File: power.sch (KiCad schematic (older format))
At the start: 6 parts

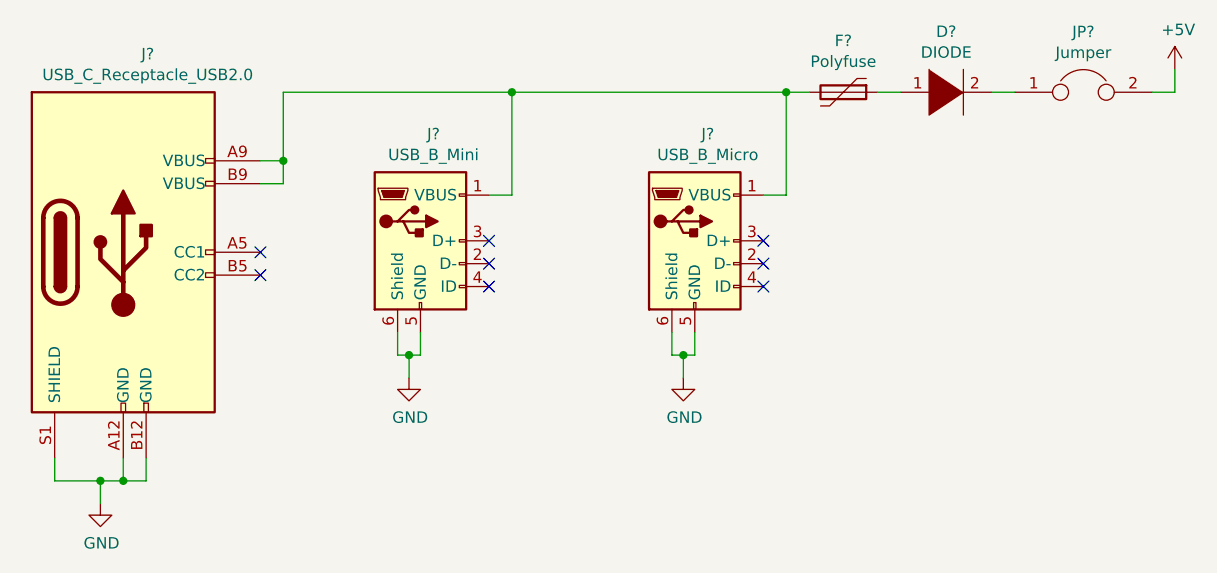
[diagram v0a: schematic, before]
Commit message: Joystick net assigned.
Signed-off-by: Kali Prasad <kprasadvnsi@protonmail.com>
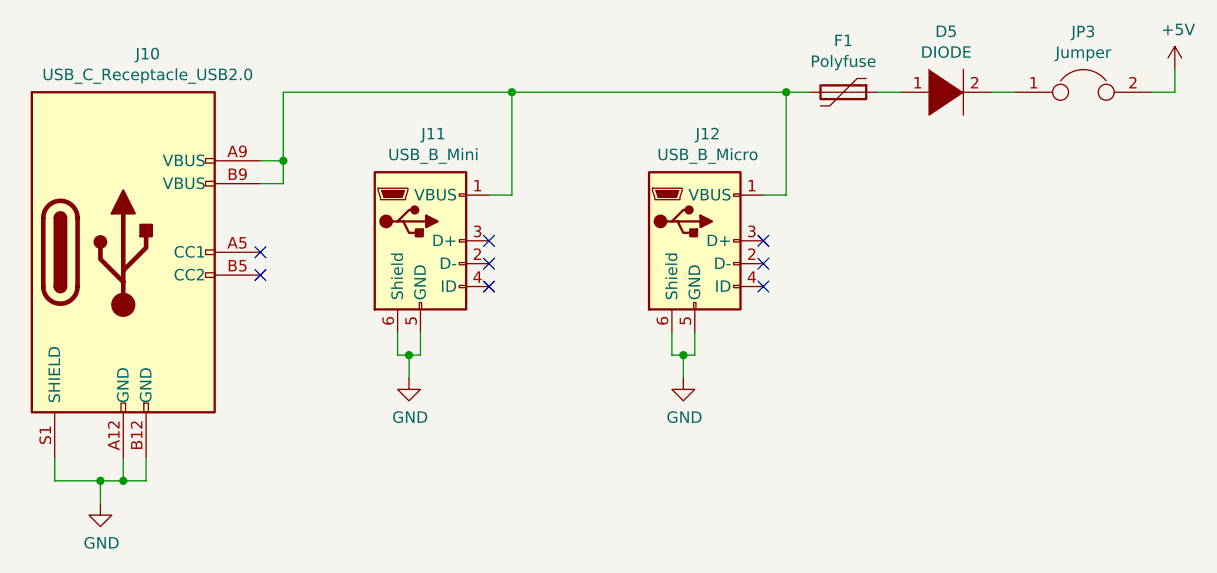
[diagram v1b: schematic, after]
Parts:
- gave numbers to parts that had none: 6
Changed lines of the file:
@@
 $EndDescr
 $Comp
-L lt_eval_board:USB_C_Receptacle_USB2.0 J?
+L lt_eval_board:USB_C_Receptacle_USB2.0 J10
 U 1 1 5D177E87
 P 3650 3950
-F 0 "J?" H 3757 4817 50  0000 C CNN
+F 0 "J10" H 3757 4817 50  0000 C CNN
 F 1 "USB_C_Receptacle_USB2.0" H 3757 4726 50  0000 C CNN
 F 2 "" H 3800 3950 50  0001 C CNN
@@
 $EndComp
 $Comp
-L Connector:USB_B_Mini J?
+L Connector:USB_B_Mini J11
 U 1 1 5D178582
 P 4950 3900
-F 0 "J?" H 5007 4367 50  0000 C CNN
+F 0 "J11" H 5007 4367 50  0000 C CNN
 F 1 "USB_B_Mini" H 5007 4276 50  0000 C CNN
 F 2 "" H 5100 3850 50  0001 C CNN
@@
 $EndComp
 $Comp
-L Connector:USB_B_Micro J?
+L Connector:USB_B_Micro J12
 U 1 1 5D178CFA
 P 6150 3900
-F 0 "J?" H 6207 4367 50  0000 C CNN
+F 0 "J12" H 6207 4367 50  0000 C CNN
 F 1 "USB_B_Micro" H 6207 4276 50  0000 C CNN
 F 2 "" H 6300 3850 50  0001 C CNN
@@
 $EndComp
 $Comp
-L power:GND #PWR?
+L power:GND #PWR045
 U 1 1 5D17D7B7
 P 3550 5050
-F 0 "#PWR?" H 3550 4800 50  0001 C CNN
+F 0 "#PWR045" H 3550 4800 50  0001 C CNN
 F 1 "GND" H 3555 4877 50  0000 C CNN
 F 2 "" H 3550 5050 50  0001 C CNN
@@
 $EndComp
 $Comp
-L power:GND #PWR?
+L power:GND #PWR046
 U 1 1 5D17DB17
 P 4900 4500
-F 0 "#PWR?" H 4900 4250 50  0001 C CNN
+F 0 "#PWR046" H 4900 4250 50  0001 C CNN
 F 1 "GND" H 4905 4327 50  0000 C CNN
 F 2 "" H 4900 4500 50  0001 C CNN
@@
 $EndComp
 $Comp
-L power:GND #PWR?
+L power:GND #PWR047
 U 1 1 5D17DE24
 P 6100 4500
-F 0 "#PWR?" H 6100 4250 50  0001 C CNN
+F 0 "#PWR047" H 6100 4250 50  0001 C CNN
 F 1 "GND" H 6105 4327 50  0000 C CNN
 F 2 "" H 6100 4500 50  0001 C CNN
@@
 $EndComp
 $Comp
-L Device:Polyfuse F?
+L Device:Polyfuse F1
 U 1 1 5D17E1F6
 P 6800 3250
-F 0 "F?" V 6575 3250 50  0000 C CNN
+F 0 "F1" V 6575 3250 50  0000 C CNN
 F 1 "Polyfuse" V 6666 3250 50  0000 C CNN
 F 2 "" H 6850 3050 50  0001 L CNN
@@
 $EndComp
 $Comp
-L pspice:DIODE D?
+L pspice:DIODE D5
 U 1 1 5D17EA5D
 P 7250 3250
-F 0 "D?" H 7250 3515 50  0000 C CNN
+F 0 "D5" H 7250 3515 50  0000 C CNN
 F 1 "DIODE" H 7250 3424 50  0000 C CNN
 F 2 "" H 7250 3250 50  0001 C CNN
@@
 	6950 3250 7050 3250
 $Comp
-L Device:Jumper JP?
+L Device:Jumper JP3
 U 1 1 5D18735E
 P 7850 3250
-F 0 "JP?" H 7850 3514 50  0000 C CNN
+F 0 "JP3" H 7850 3514 50  0000 C CNN
 F 1 "Jumper" H 7850 3423 50  0000 C CNN
 F 2 "" H 7850 3250 50  0001 C CNN
@@
 	7450 3250 7550 3250
 $Comp
-L power:+5V #PWR?
+L power:+5V #PWR048
 U 1 1 5D188A9B
 P 8250 3150
-F 0 "#PWR?" H 8250 3000 50  0001 C CNN
+F 0 "#PWR048" H 8250 3000 50  0001 C CNN
 F 1 "+5V" H 8265 3323 50  0000 C CNN
 F 2 "" H 8250 3150 50  0001 C CNN
